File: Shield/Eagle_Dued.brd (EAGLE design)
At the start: 119.9 x 99.8 mm, 76 parts, among them IC1 7805TV, IC2 LM340MP-05

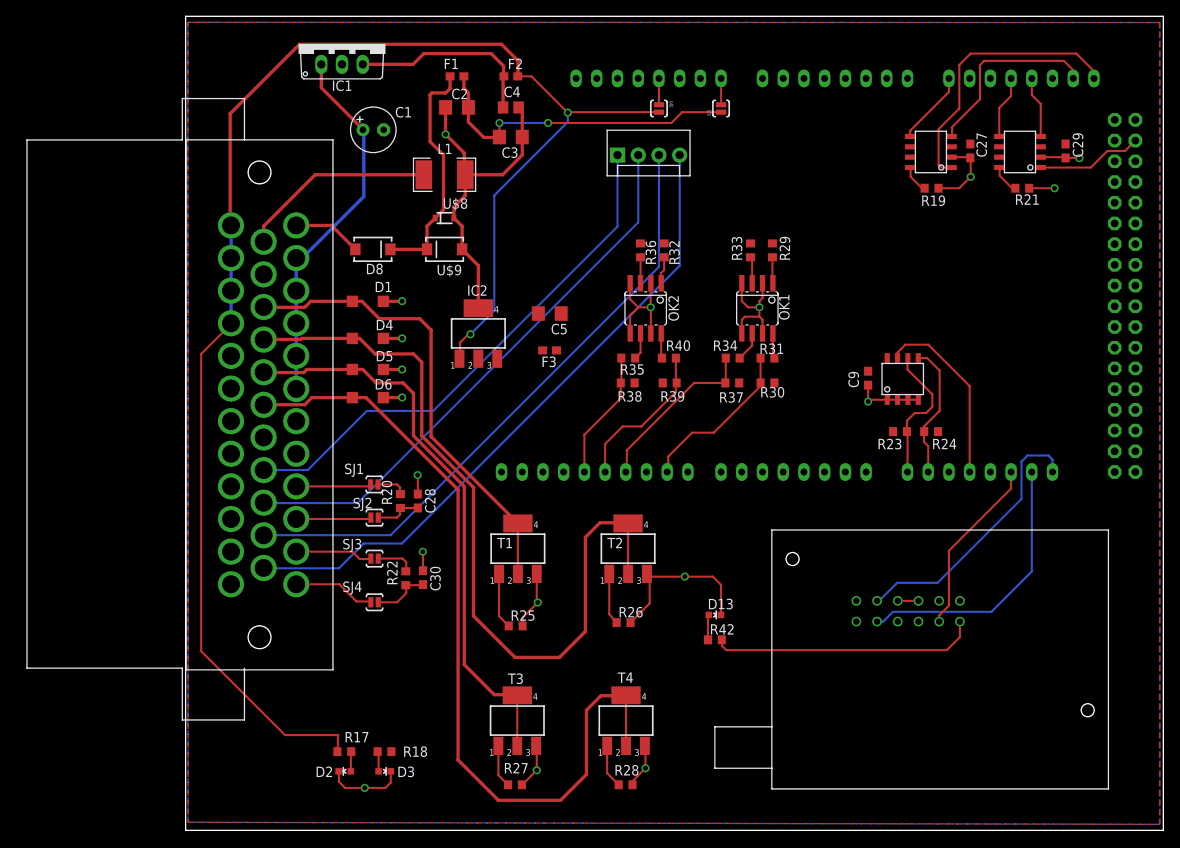
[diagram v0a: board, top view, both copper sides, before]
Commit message: Newer version of analog board, new version of DueD
Dued board now properly sized for the new case.
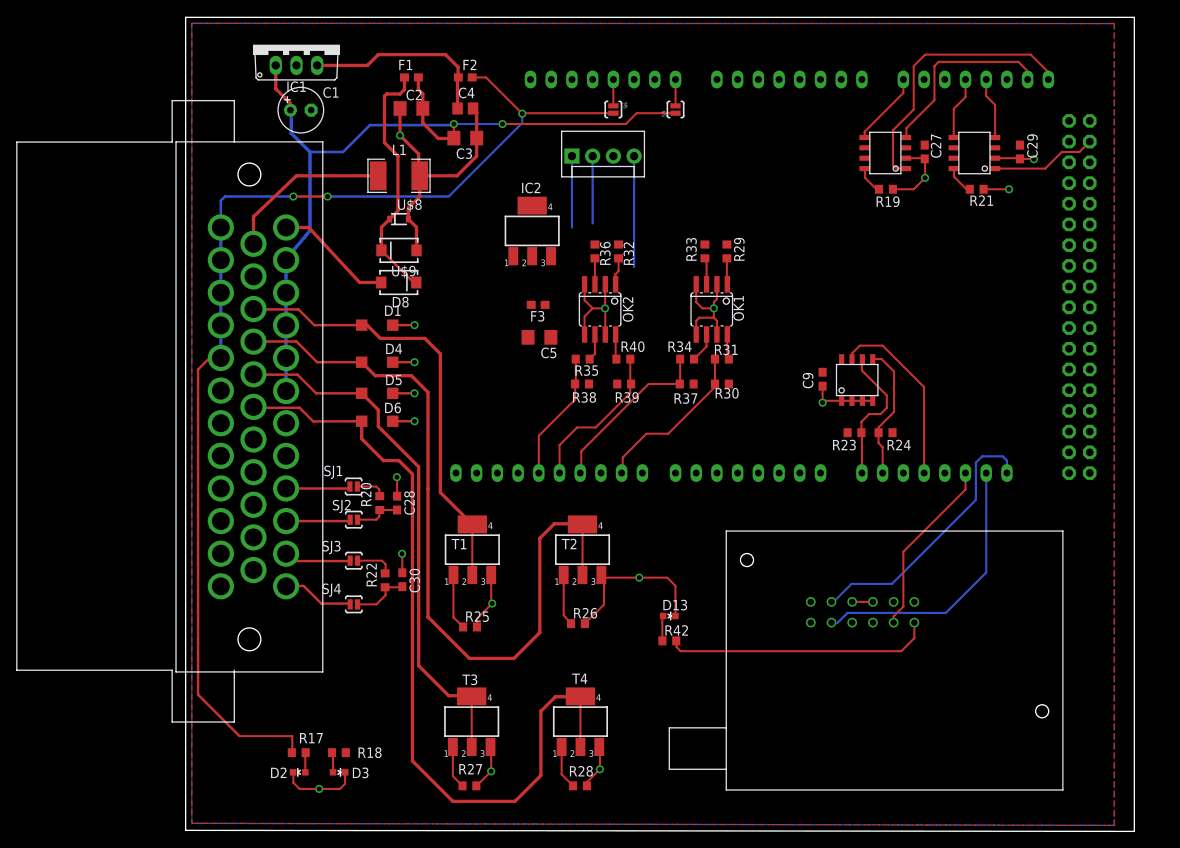
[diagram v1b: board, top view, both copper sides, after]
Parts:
- moved IC2 14.2 mm to (42.5, 73.5)
- moved C1 9.21 mm to (14.1, 88.3)
- moved F3 5.76 mm to (43.2, 64.4)
- moved COMMUNICATION 5.59 mm to (91.8, 43.8)
- moved D13 5.59 mm to (59.3, 26.3)
- moved PWML 5.59 mm to (69.0, 43.8)
- moved R23 5.59 mm to (82.0, 48.8)
- moved R29 5.59 mm to (66.4, 71.0)
- moved R30 5.59 mm to (65.8, 57.8)
- moved R42 5.59 mm to (59.3, 23.2)
- moved SJ5 5.59 mm to (60.1, 88.4)
- moved U$5 5.59 mm to (79.8, 53.3)
- moved ADCH 5.59 mm to (96.9, 92.1)
- moved ADCL 5.59 mm to (74.0, 92.1)
- moved R19 5.59 mm to (85.9, 78.6)
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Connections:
- removed net +5V\: U$3.28
- net +5V: now also U$3.28
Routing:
- net AIN3: track 75.8 -> 0.00 mm
- net AIN4: track 80.0 -> 13.6 mm
- net AIN2: track 68.5 -> 8.26 mm
- net AIN1: track 64.5 -> 8.76 mm
- net +5V: track 186.9 -> 139.4 mm, vias 2 -> 3
- net +12V: track 85.7 -> 101.7 mm
- net GND: track 158.8 -> 152.2 mm
- net V_IN: track 8.46 -> 14.6 mm
- net MOSFET3: track 69.9 -> 66.2 mm
- net DGND: track 24.2 -> 20.6 mm
- net N$3: track 29.2 -> 30.6 mm
- net MOSFET2: track 95.9 -> 94.5 mm
- net MOSFET4: track 100.8 -> 99.4 mm
- net CANH1: track 9.55 -> 8.19 mm
- net CANH0: track 9.23 -> 7.93 mm
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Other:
- board size 119.9 x 99.8 mm -> 116.3 x 99.8 mm
